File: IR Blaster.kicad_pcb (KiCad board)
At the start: 2 copper layers, 47.8 x 35.8 mm, 54 parts, among them CON1 AVR-ISP-6, IC1 ATMEGA328P-A, P1 FTDI Header, P2 IR Receiver, P3 Analog IN, P4 PWR, Q1 FDV303N, U1 ATSHA204A, U2 NRF24L01, U3 AT25DF512C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

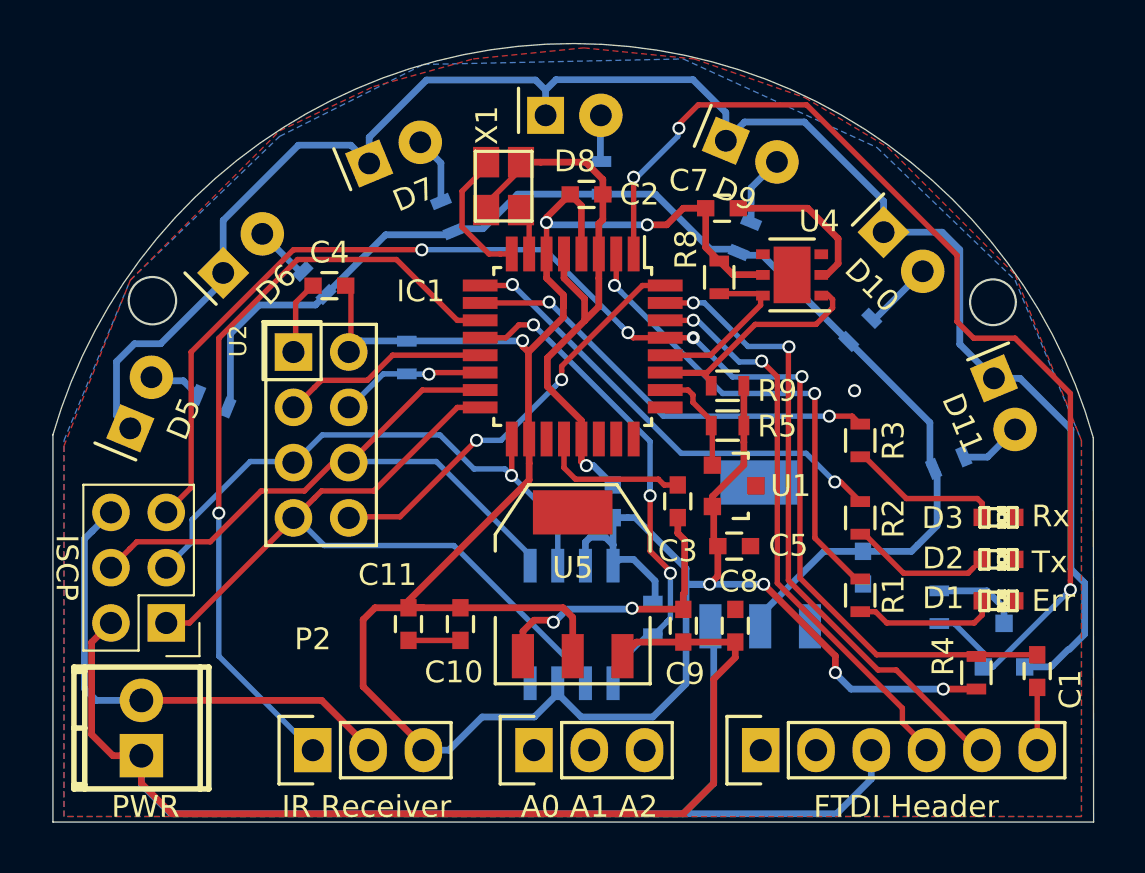
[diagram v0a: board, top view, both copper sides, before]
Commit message: Increased higher-current trace widths to ensure ample current to higher-drain parts such as the LEDs.
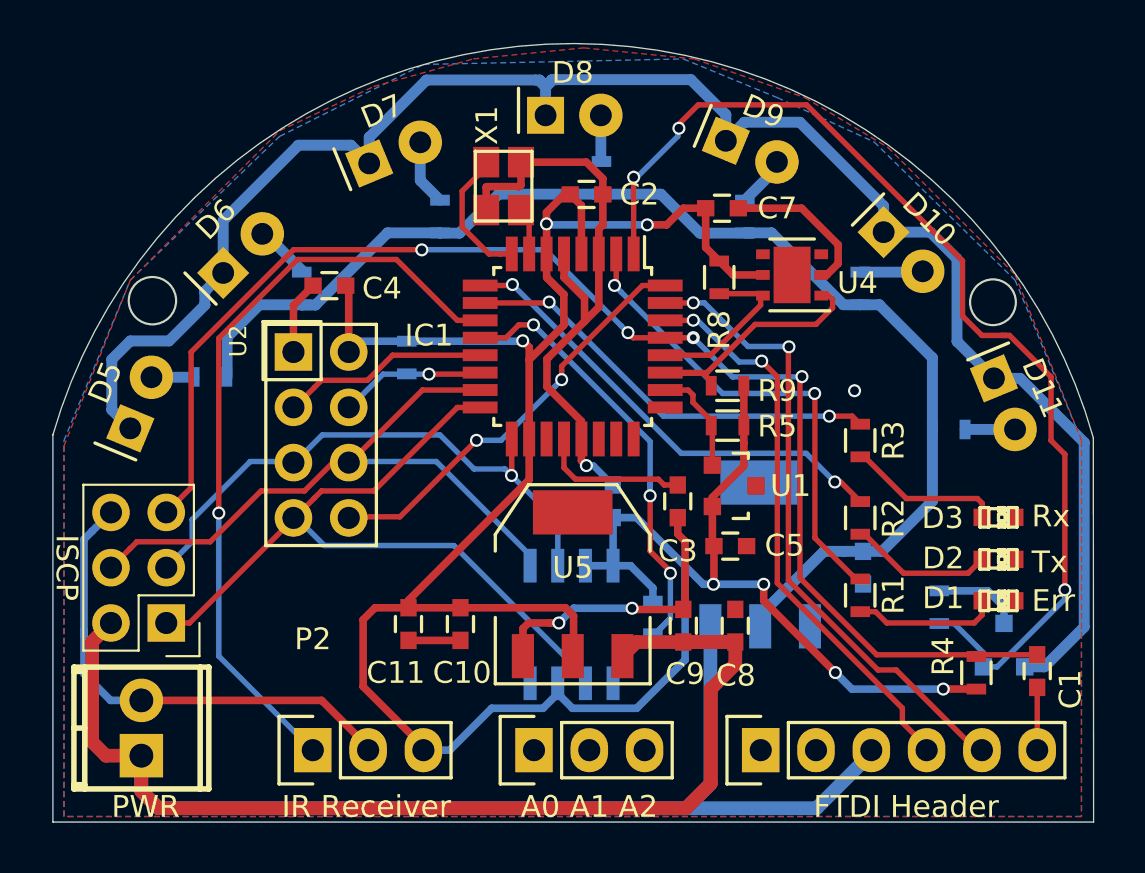
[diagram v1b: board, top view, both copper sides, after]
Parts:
- moved R16 1.90 mm to (147.8, 90.0), turned to 90 degrees
- moved R17 1.52 mm to (151.9, 96.5), turned to 0 degrees
- moved R11 1.12 mm to (118.0, 94.1), turned to 180 degrees
- moved R15 0.96 mm to (142.5, 86.7), turned to 90 degrees
- moved R12 0.64 mm to (122.2, 90.0), turned to 90 degrees
- moved R13 0.33 mm to (128.5, 86.7), turned to 90 degrees
- moved C5 0.18 mm to (141.9, 101.9)
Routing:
- net VCC: track 100.0 -> 103.9 mm
- net +3V3: track 132.6 -> 129.3 mm
- net Net-(D10-Pad1): track 81.8 -> 84.3 mm
- net GND: track 81.6 -> 83.7 mm
- net Net-(D8-Pad2): track 2.12 -> 4.25 mm
- net Net-(D9-Pad2): track 3.60 -> 2.70 mm
- net /D8: track 24.1 -> 25.0 mm
- net Net-(D11-Pad2): track 2.89 -> 2.30 mm
- net Net-(D2-Pad2): track 6.05 -> 6.59 mm
- net /MISO: track 35.7 -> 35.2 mm
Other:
- net class 1A: trace_width 0.31 -> 0.5
- net class 3V3 added: clearance 0.2, trace_width 0.35, via_dia 0.6, via_drill 0.4
- net class VCC added: clearance 0.2, trace_width 0.63, via_dia 0.65, via_drill 0.4

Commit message: Added some modest via stitching to the ground planes.
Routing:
- net GND: track 83.7 -> 136.8 mm, vias 3 -> 41
